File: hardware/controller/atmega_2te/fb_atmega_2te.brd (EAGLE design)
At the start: 30.5 x 58.2 mm, 51 parts, among them IC1 ATMEGA 328P/168P, IC2 MC34063AP, Q1 8 MHz, T1 BC557, T2 BC547, T3 BC640

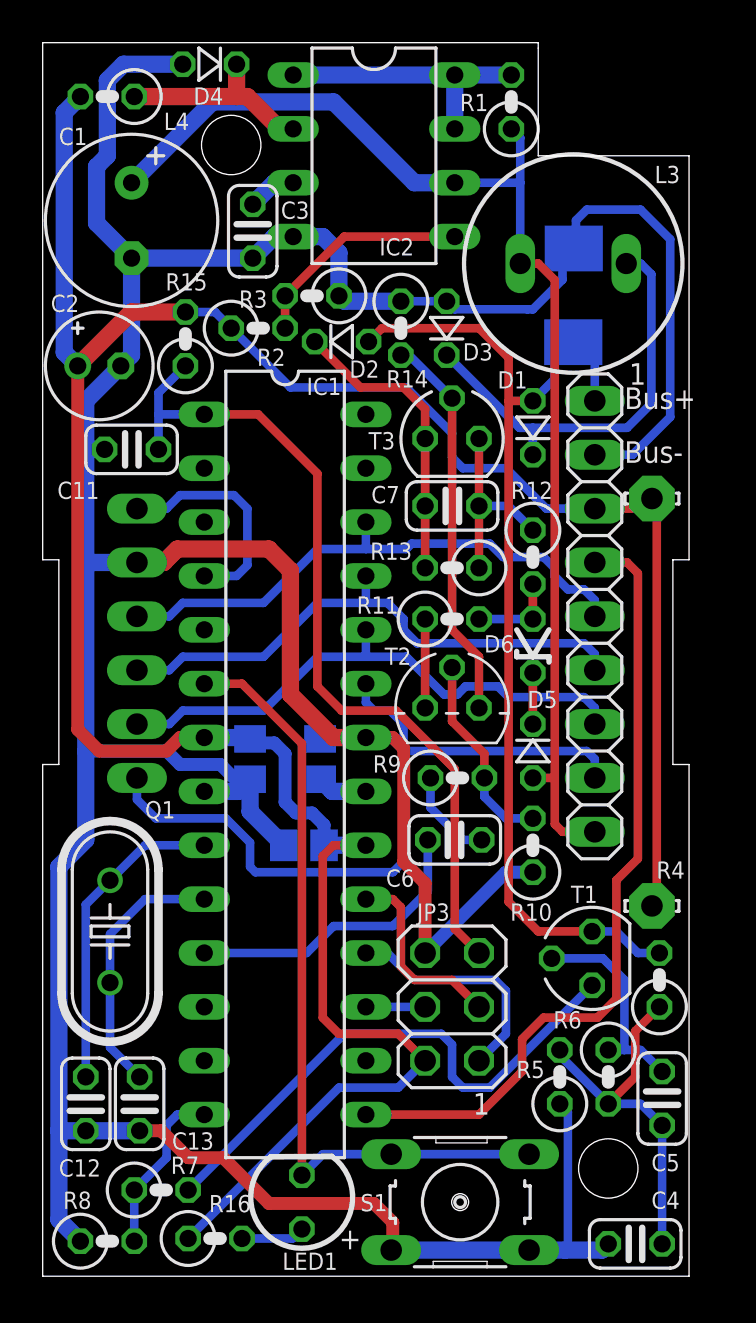
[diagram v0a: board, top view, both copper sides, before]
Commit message: Upgraded fb_atmega_2te to version 1.1
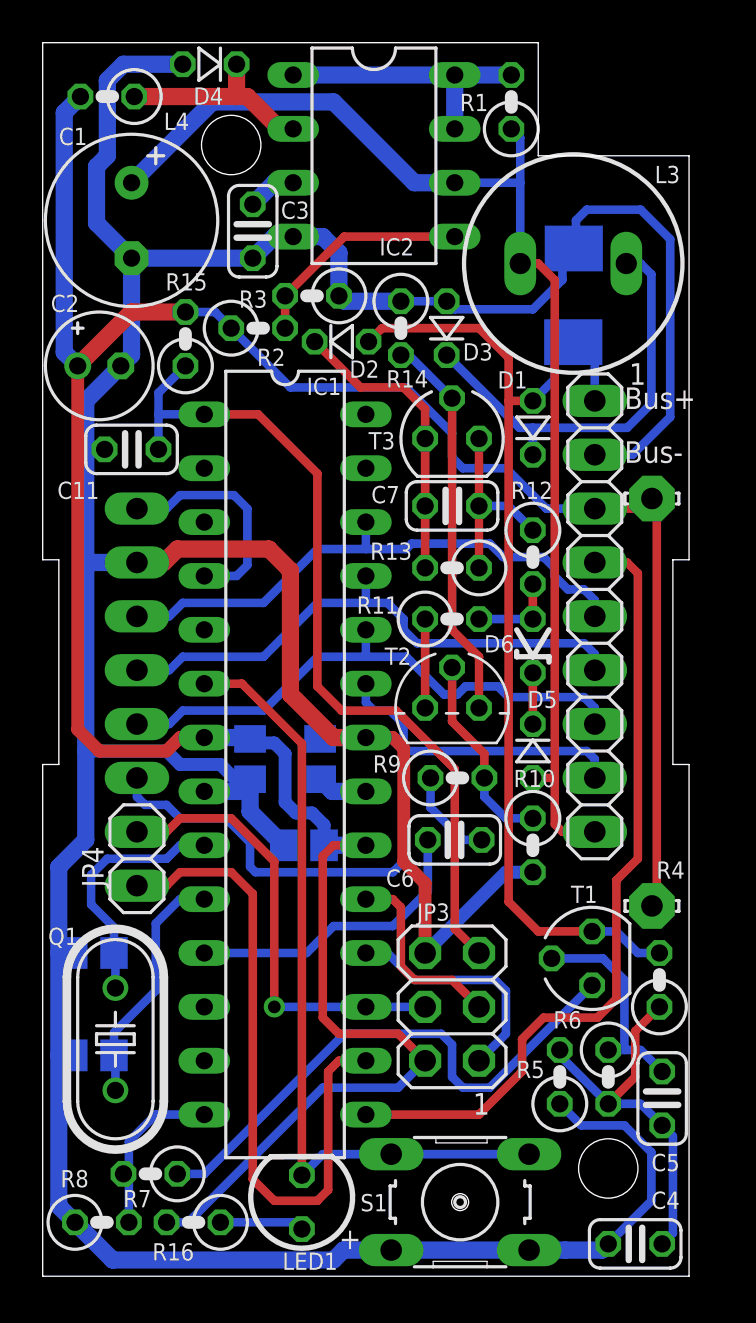
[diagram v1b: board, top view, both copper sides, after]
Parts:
- added JP4: für 2 Kanal PWM, pinhead:1X02
- C12, C13: device rcl:C025-024X044 -> rcl:C0805
- moved C12 7.12 mm to (2.41, 15.2), flipped to the bottom, turned to 0 degrees
- moved Q1 5.09 mm to (3.43, 11.2)
- moved C13 3.14 mm to (2.41, 10.4), flipped to the bottom, turned to 0 degrees
- moved R16 1.27 mm to (7.11, 2.54), turned to 180 degrees
- moved R8 0.92 mm to (2.79, 2.54)
- moved R7 0.92 mm to (5.08, 4.83), turned to 180 degrees
- turned R10 to 270 degrees
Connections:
- removed net MOSI: IC1.17, JP3.4
- removed net SS: IC1.16
- new net MOSI/OC2A: IC1.17, JP3.4, JP4.2
- new net OC1B: IC1.16, JP4.1
- net +3V3: now also R16.2; no longer R16.1
- net EIB_IN: now also R7.2; no longer R7.1
- net GND: now also R10.2; no longer R10.1
- net N$14: now also R7.1; no longer R7.2
- net N$20: now also R10.1; no longer R10.2
- net N$9: now also R16.1; no longer R16.2
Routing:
- net OC1B: track 0.00 -> 31.4 mm
- net MOSI/OC2A: track 0.00 -> 21.6 mm, vias 0 -> 1
- net N$39: track 14.9 -> 11.8 mm
- net MOSI: track 2.79 -> 0.00 mm
- net N$9: track 3.01 -> 3.97 mm
- net N$38: track 12.4 -> 11.5 mm
- net GND: track 199.4 -> 200.3 mm
- net +3V3: track 131.1 -> 131.8 mm
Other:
- outline, holes or cut-outs redrawn

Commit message: Upgraded fb_atmega_2te to version 1.2
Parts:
- turned L4 to 0 degrees
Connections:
- net +3V3: now also L4.1; no longer L4.2
- net N$26: now also L4.2; no longer L4.1
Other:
- board text added: "-"
- board text added: "Bus"
- board text removed: "Bus+"
- board text removed: "Bus-"
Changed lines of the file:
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@@
 <?xml version="1.0" encoding="utf-8"?>
 <!DOCTYPE eagle SYSTEM "eagle.dtd">
-<eagle version="6.4">
+<eagle version="6.3">
 <drawing>
 <settings>
@@
 <layer number="25" name="tNames" color="7" fill="1" visible="yes" active="yes"/>
 <layer number="26" name="bNames" color="7" fill="1" visible="yes" active="yes"/>
-<layer number="27" name="tValues" color="7" fill="1" visible="yes" active="yes"/>
-<layer number="28" name="bValues" color="7" fill="1" visible="yes" active="yes"/>
+<layer number="27" name="tValues" color="7" fill="1" visible="no" active="yes"/>
+<layer number="28" name="bValues" color="7" fill="1" visible="no" active="yes"/>
 <layer number="29" name="tStop" color="7" fill="3" visible="no" active="yes"/>
 <layer number="30" name="bStop" color="7" fill="6" visible="no" active="yes"/>
@@
 <hole x="8.8898" y="53.3401" drill="2.8"/>
 <hole x="19.685" y="3.4925" drill="0.8"/>
-<text x="27.432" y="40.894" size="1.016" layer="21">Bus+</text>
-<text x="27.432" y="38.354" size="1.016" layer="21">Bus-</text>
+<text x="28.194" y="41.148" size="1.016" layer="21">+</text>
 <text x="21.082" y="8.636" size="1.016" layer="21" rot="R180">1</text>
 <text x="13.97" y="1.27" size="1.016" layer="21">+</text>
@@
 <wire x1="0.762" y1="24.13" x2="0" y2="24.13" width="0.0254" layer="20"/>
 <wire x1="0" y1="24.13" x2="0" y2="0" width="0.0254" layer="20"/>
+<text x="28.448" y="37.846" size="1.016" layer="21">-</text>
+<text x="28.956" y="38.608" size="1.016" layer="21" rot="R90">Bus</text>
 </plain>
 <attributes>
@@
 <elements>
 <element name="S1" library="switch-omron" package="B3F-10XX" value="Programmier Taster" x="19.6849" y="3.4926" locked="yes" smashed="yes" rot="R180">
-<attribute name="NAME" x="16.2558" y="3.8737" size="0.8128" layer="25" ratio="10" rot="R180"/>
+<attribute name="NAME" x="24.6378" y="3.8737" size="0.8128" layer="25" ratio="10" rot="R180"/>
 <attribute name="OC_NEWARK" value="36M3542" x="19.6849" y="3.4926" size="1.778" layer="27" rot="R180" display="off"/>
 <attribute name="MPN" value="B3F-1000" x="19.6849" y="3.4926" size="1.778" layer="27" rot="R180" display="off"/>
@@
 </element>
 <element name="C6" library="rcl" package="C025-024X044" value="10nF" x="19.431" y="20.574" smashed="yes" rot="R180">
-<attribute name="NAME" x="17.526" y="19.177" size="0.8128" layer="25" ratio="10" rot="R180"/>
+<attribute name="NAME" x="20.066" y="19.177" size="0.8128" layer="25" ratio="10" rot="R180"/>
 </element>
 <element name="R9" library="rcl" package="0207/2V" value="5k6" x="19.558" y="23.495" smashed="yes">
-<attribute name="NAME" x="15.5702" y="23.749" size="0.8128" layer="25" ratio="10"/>
+<attribute name="NAME" x="19.6342" y="21.971" size="0.8128" layer="25" ratio="10"/>
 </element>
 <element name="R10" library="rcl" package="0207/2V" value="100k" x="23.114" y="20.32" smashed="yes" rot="R270">
-<attribute name="NAME" x="24.1808" y="23.876" size="0.8128" layer="25" ratio="10" rot="R180"/>
+<attribute name="NAME" x="23.9268" y="18.034" size="0.8128" layer="25" ratio="10" rot="R180"/>
 </element>
 <element name="IC2" library="mc34063" package="DIL08" value="MC34063AP" x="15.621" y="52.832" smashed="yes" rot="R270">
@@
 </element>
 <element name="R15" library="rcl" package="0207/2V" value="10k" x="6.731" y="44.196" smashed="yes" rot="R90">
-<attribute name="NAME" x="5.7912" y="46.482" size="0.8128" layer="25" ratio="10"/>
+<attribute name="NAME" x="6.2992" y="46.482" size="0.8128" layer="25" ratio="10"/>
 </element>
 <element name="C11" library="rcl" package="C025-024X044" value="100nF" x="4.191" y="38.989" smashed="yes">
@@
 </element>
 <element name="D4" library="diode" package="D-2.5" value="BAT46" x="7.874" y="57.15" smashed="yes" rot="R180">
-<attribute name="NAME" x="7.112" y="55.245" size="0.8128" layer="25" ratio="10"/>
+<attribute name="NAME" x="6.604" y="55.245" size="0.8128" layer="25" ratio="10"/>
 </element>
 <element name="D1" library="diode" package="D-2.5" value="1N4148" x="23.114" y="40.005" smashed="yes" rot="R90">
@@
 <attribute name="VALUE" x="28.269" y="50.752" size="0.8128" layer="27" rot="R180"/>
 </element>
-<element name="L4" library="rcl" package="0207/2V" value="220µ" x="3.048" y="55.626" smashed="yes" rot="R180">
-<attribute name="NAME" x="6.9088" y="54.864" size="0.8128" layer="25" ratio="10" rot="R180"/>
-<attribute name="VALUE" x="3.3528" y="57.6072" size="0.8128" layer="27" ratio="10" rot="R180"/>
+<element name="L4" library="rcl" package="0207/2V" value="220µ" x="3.048" y="55.626" smashed="yes">
+<attribute name="NAME" x="2.7432" y="56.896" size="0.8128" layer="25" ratio="10"/>
+<attribute name="VALUE" x="2.7432" y="53.6448" size="0.8128" layer="27" ratio="10"/>
 </element>
 <element name="Q1" library="crystal" package="HC49U-V" value="8 MHz" x="3.429" y="11.176" smashed="yes" rot="R270">
@@
 <contactref element="IC2" pad="2"/>
 <contactref element="D4" pad="C"/>
-<contactref element="L4" pad="1"/>
+<contactref element="L4" pad="2"/>
 <wire x1="4.318" y1="55.626" x2="9.144" y2="55.626" width="0.8128" layer="1"/>
 <wire x1="9.144" y1="55.626" x2="9.652" y2="55.626" width="0.8128" layer="1"/>
@@
 <contactref element="C2" pad="+"/>
 <contactref element="R2" pad="1"/>
-<contactref element="L4" pad="2"/>
+<contactref element="L4" pad="1"/>
 <contactref element="IC1" pad="7"/>
 <contactref element="C8" pad="1"/>
